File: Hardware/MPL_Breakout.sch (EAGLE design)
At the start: 9 parts

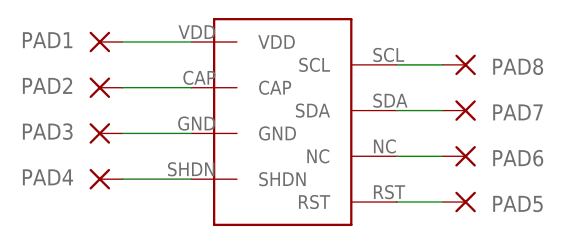
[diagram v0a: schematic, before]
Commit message: updated pinheaders and names
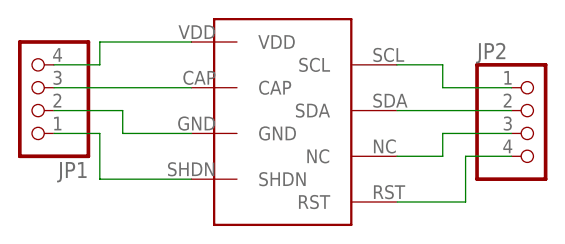
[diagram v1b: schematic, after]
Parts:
- removed PAD1, PAD2, PAD3, PAD4, PAD5, PAD6, PAD7, PAD8: (no value), wirepad:1,6/0,8
- added JP1, JP2: (no value), pinhead:PINHD-1X4
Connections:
- net N$1: now also JP1.4; no longer PAD1.P
- net N$2: now also JP1.3; no longer PAD2.P
- net N$3: now also JP1.2; no longer PAD3.P
- net N$4: now also JP1.1; no longer PAD4.P
- net N$5: now also JP2.4; no longer PAD5.P
- net N$6: now also JP2.3; no longer PAD6.P
- net N$7: now also JP2.2; no longer PAD7.P
- net N$8: now also JP2.1; no longer PAD8.P
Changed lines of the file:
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@@
 <parts>
 <part name="B1" library="MPL115A2T1" deviceset="MPL115A2T1" device=""/>
-<part name="PAD1" library="wirepad" library_urn="urn:adsk.eagle:library:412" deviceset="1,6/0,8" device="" package3d_urn="urn:adsk.eagle:package:30830/1"/>
-<part name="PAD2" library="wirepad" library_urn="urn:adsk.eagle:library:412" deviceset="1,6/0,8" device="" package3d_urn="urn:adsk.eagle:package:30830/1"/>
-<part name="PAD3" library="wirepad" library_urn="urn:adsk.eagle:library:412" deviceset="1,6/0,8" device="" package3d_urn="urn:adsk.eagle:package:30830/1"/>
-<part name="PAD4" library="wirepad" library_urn="urn:adsk.eagle:library:412" deviceset="1,6/0,8" device="" package3d_urn="urn:adsk.eagle:package:30830/1"/>
-<part name="PAD5" library="wirepad" library_urn="urn:adsk.eagle:library:412" deviceset="1,6/0,8" device="" package3d_urn="urn:adsk.eagle:package:30830/1"/>
-<part name="PAD6" library="wirepad" library_urn="urn:adsk.eagle:library:412" deviceset="1,6/0,8" device="" package3d_urn="urn:adsk.eagle:package:30830/1"/>
-<part name="PAD7" library="wirepad" library_urn="urn:adsk.eagle:library:412" deviceset="1,6/0,8" device="" package3d_urn="urn:adsk.eagle:package:30830/1"/>
-<part name="PAD8" library="wirepad" library_urn="urn:adsk.eagle:library:412" deviceset="1,6/0,8" device="" package3d_urn="urn:adsk.eagle:package:30830/1"/>
+<part name="JP1" library="pinhead" library_urn="urn:adsk.eagle:library:325" deviceset="PINHD-1X4" device="" package3d_urn="urn:adsk.eagle:package:22407/2"/>
+<part name="JP2" library="pinhead" library_urn="urn:adsk.eagle:library:325" deviceset="PINHD-1X4" device="" package3d_urn="urn:adsk.eagle:package:22407/2"/>
 </parts>
 <sheets>
@@
 <instances>
 <instance part="B1" gate="G$1" x="22.86" y="15.24" smashed="yes"/>
-<instance part="PAD1" gate="P" x="0" y="27.94" smashed="yes">
-<attribute name="NAME" x="-8.763" y="27.2542" size="1.778" layer="95"/>
-<attribute name="VALUE" x="-1.143" y="24.638" size="1.778" layer="96"/>
+<instance part="JP1" gate="A" x="-7.62" y="22.86" smashed="yes" rot="R180">
+<attribute name="NAME" x="-1.27" y="14.605" size="1.778" layer="95" rot="R180"/>
+<attribute name="VALUE" x="-1.27" y="30.48" size="1.778" layer="96" rot="R180"/>
 </instance>
-<instance part="PAD2" gate="P" x="0" y="22.86" smashed="yes">
-<attribute name="NAME" x="-8.763" y="22.1742" size="1.778" layer="95"/>
-<attribute name="VALUE" x="-1.143" y="19.558" size="1.778" layer="96"/>
-</instance>
-<instance part="PAD3" gate="P" x="0" y="17.78" smashed="yes">
-<attribute name="NAME" x="-8.763" y="17.0942" size="1.778" layer="95"/>
-<attribute name="VALUE" x="-1.143" y="14.478" size="1.778" layer="96"/>
-</instance>
-<instance part="PAD4" gate="P" x="0" y="12.7" smashed="yes">
-<attribute name="NAME" x="-8.763" y="12.0142" size="1.778" layer="95"/>
-<attribute name="VALUE" x="-1.143" y="9.398" size="1.778" layer="96"/>
-</instance>
-<instance part="PAD5" gate="P" x="40.64" y="10.16" smashed="yes" rot="R180">
-<attribute name="NAME" x="49.403" y="10.8458" size="1.778" layer="95" rot="R180"/>
-<attribute name="VALUE" x="41.783" y="13.462" size="1.778" layer="96" rot="R180"/>
-</instance>
-<instance part="PAD6" gate="P" x="40.64" y="15.24" smashed="yes" rot="R180">
-<attribute name="NAME" x="49.403" y="15.9258" size="1.778" layer="95" rot="R180"/>
-<attribute name="VALUE" x="41.783" y="18.542" size="1.778" layer="96" rot="R180"/>
-</instance>
-<instance part="PAD7" gate="P" x="40.64" y="20.32" smashed="yes" rot="R180">
-<attribute name="NAME" x="49.403" y="21.0058" size="1.778" layer="95" rot="R180"/>
-<attribute name="VALUE" x="41.783" y="23.622" size="1.778" layer="96" rot="R180"/>
-</instance>
-<instance part="PAD8" gate="P" x="40.64" y="25.4" smashed="yes" rot="R180">
-<attribute name="NAME" x="49.403" y="26.0858" size="1.778" layer="95" rot="R180"/>
-<attribute name="VALUE" x="41.783" y="28.702" size="1.778" layer="96" rot="R180"/>
+<instance part="JP2" gate="A" x="48.26" y="17.78" smashed="yes">
+<attribute name="NAME" x="41.91" y="26.035" size="1.778" layer="95"/>
+<attribute name="VALUE" x="41.91" y="10.16" size="1.778" layer="96"/>
 </instance>
 </instances>
@@
 <net name="N$1" class="0">
 <segment>
-<pinref part="PAD1" gate="P" pin="P"/>
 <pinref part="B1" gate="G$1" pin="VDD"/>
-<wire x1="2.54" y1="27.94" x2="10.16" y2="27.94" width="0.1524" layer="91"/>
+<wire x1="0" y1="27.94" x2="10.16" y2="27.94" width="0.1524" layer="91"/>
+<wire x1="0" y1="27.94" x2="0" y2="25.4" width="0.1524" layer="91"/>
+<pinref part="JP1" gate="A" pin="4"/>
+<wire x1="0" y1="25.4" x2="-5.08" y2="25.4" width="0.1524" layer="91"/>
 </segment>
 </net>
 <net name="N$2" class="0">
 <segment>
-<pinref part="PAD2" gate="P" pin="P"/>
 <pinref part="B1" gate="G$1" pin="CAP"/>
-<wire x1="2.54" y1="22.86" x2="10.16" y2="22.86" width="0.1524" layer="91"/>
+<pinref part="JP1" gate="A" pin="3"/>
+<wire x1="10.16" y1="22.86" x2="-5.08" y2="22.86" width="0.1524" layer="91"/>
 </segment>
 </net>
 <net name="N$3" class="0">
 <segment>
-<pinref part="PAD3" gate="P" pin="P"/>
 <pinref part="B1" gate="G$1" pin="GND"/>
 <wire x1="2.54" y1="17.78" x2="10.16" y2="17.78" width="0.1524" layer="91"/>
+<wire x1="2.54" y1="17.78" x2="2.54" y2="20.32" width="0.1524" layer="91"/>
+<pinref part="JP1" gate="A" pin="2"/>
+<wire x1="2.54" y1="20.32" x2="-5.08" y2="20.32" width="0.1524" layer="91"/>
 </segment>
 </net>
 <net name="N$4" class="0">
 <segment>
-<pinref part="PAD4" gate="P" pin="P"/>
 <pinref part="B1" gate="G$1" pin="SHDN"/>
-<wire x1="2.54" y1="12.7" x2="10.16" y2="12.7" width="0.1524" layer="91"/>
+<wire x1="0" y1="12.7" x2="10.16" y2="12.7" width="0.1524" layer="91"/>
+<wire x1="0" y1="12.7" x2="0" y2="17.78" width="0.1524" layer="91"/>
+<pinref part="JP1" gate="A" pin="1"/>
+<wire x1="0" y1="17.78" x2="-5.08" y2="17.78" width="0.1524" layer="91"/>
 </segment>
 </net>
 <net name="N$5" class="0">
 <segment>
-<pinref part="PAD5" gate="P" pin="P"/>
 <pinref part="B1" gate="G$1" pin="RST"/>
-<wire x1="38.1" y1="10.16" x2="33.02" y2="10.16" width="0.1524" layer="91"/>
+<wire x1="40.64" y1="10.16" x2="33.02" y2="10.16" width="0.1524" layer="91"/>
+<wire x1="40.64" y1="10.16" x2="40.64" y2="15.24" width="0.1524" layer="91"/>
+<pinref part="JP2" gate="A" pin="4"/>
+<wire x1="40.64" y1="15.24" x2="45.72" y2="15.24" width="0.1524" layer="91"/>
 </segment>
 </net>
 <net name="N$6" class="0">
 <segment>
-<pinref part="PAD6" gate="P" pin="P"/>
 <pinref part="B1" gate="G$1" pin="NC"/>
 <wire x1="38.1" y1="15.24" x2="33.02" y2="15.24" width="0.1524" layer="91"/>
+<wire x1="38.1" y1="15.24" x2="38.1" y2="17.78" width="0.1524" layer="91"/>
+<pinref part="JP2" gate="A" pin="3"/>
+<wire x1="38.1" y1="17.78" x2="45.72" y2="17.78" width="0.1524" layer="91"/>
 </segment>
 </net>
 <net name="N$7" class="0">
 <segment>
-<pinref part="PAD7" gate="P" pin="P"/>
 <pinref part="B1" gate="G$1" pin="SDA"/>
-<wire x1="38.1" y1="20.32" x2="33.02" y2="20.32" width="0.1524" layer="91"/>
+<pinref part="JP2" gate="A" pin="2"/>
+<wire x1="33.02" y1="20.32" x2="45.72" y2="20.32" width="0.1524" layer="91"/>
 </segment>
 </net>
 <net name="N$8" class="0">
 <segment>
-<pinref part="PAD8" gate="P" pin="P"/>
 <pinref part="B1" gate="G$1" pin="SCL"/>
 <wire x1="38.1" y1="25.4" x2="33.02" y2="25.4" width="0.1524" layer="91"/>
+<wire x1="38.1" y1="25.4" x2="38.1" y2="22.86" width="0.1524" layer="91"/>
+<pinref part="JP2" gate="A" pin="1"/>
+<wire x1="38.1" y1="22.86" x2="45.72" y2="22.86" width="0.1524" layer="91"/>
 </segment>
 </net>
